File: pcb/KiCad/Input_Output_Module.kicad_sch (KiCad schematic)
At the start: 49 parts, among them J11 Curr_In (Out2), J12 Error_In, J13 Curr_Out (Out2), J14 Error_Out (In1), J16 Error_Mon, J3 Piezo_In (Out1), J5 Piezo_Out, J7 Piezo_Monitor, U4 OPA1604, U5 BUF634, U7 OPA1602, U8 OPA1602

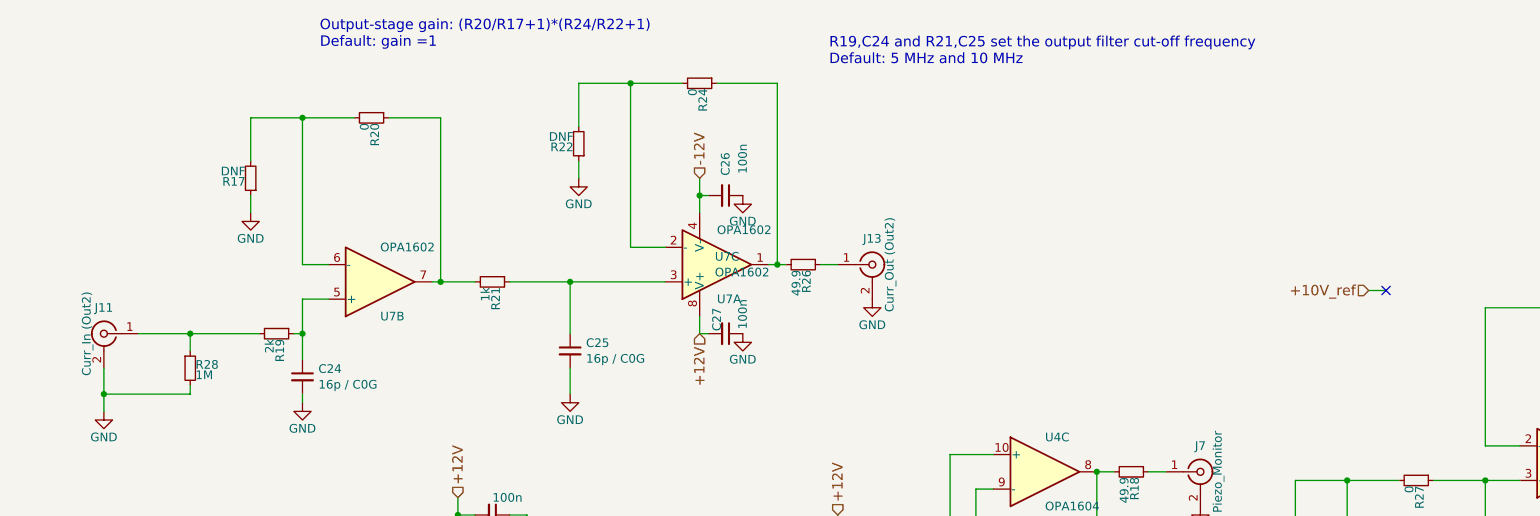
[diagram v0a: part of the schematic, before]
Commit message: Remove RedPitaya offset voltage at out2
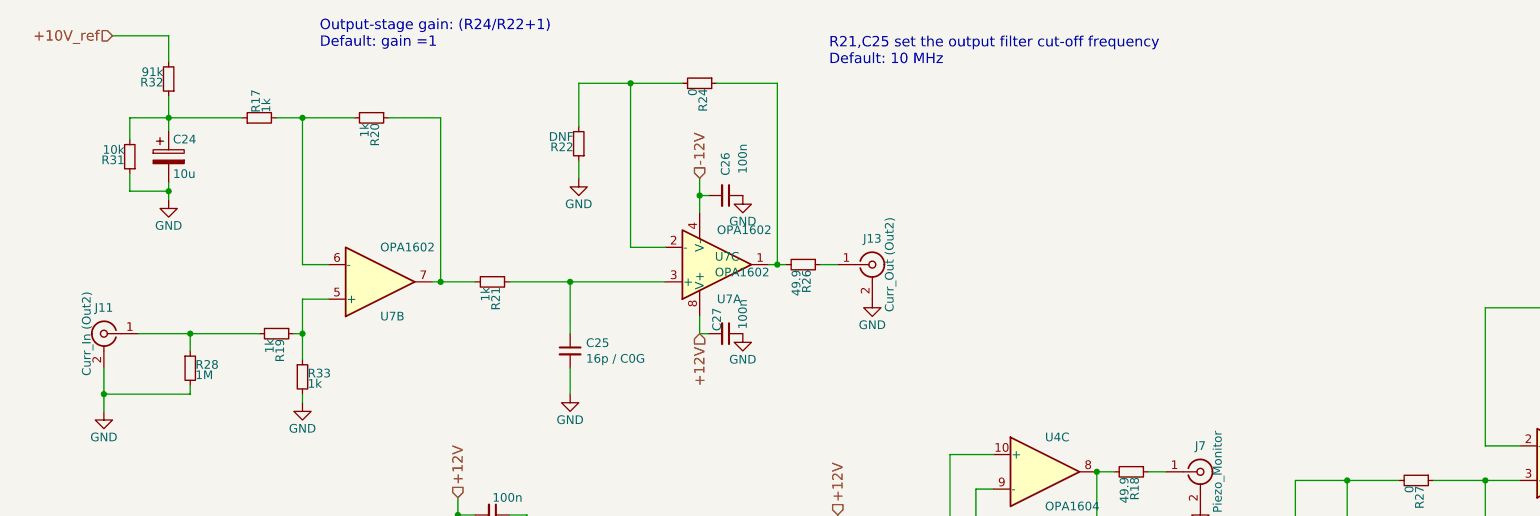
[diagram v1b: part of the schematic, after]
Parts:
- removed C24: 16p / C0G, Capacitor_SMD:C_0603_1608Metric, symbol Device:C_Small
- added C24: 10u, Capacitor_Tantalum_SMD:CP_EIA-3528-21_Kemet-B, symbol Device:C_Polarized
- added R31: 10k, Resistor_SMD:R_0603_1608Metric, symbol Device:R_Small
- added R32: 91k, Resistor_SMD:R_0603_1608Metric, symbol Device:R_Small
- added R33: 1k, Resistor_SMD:R_0603_1608Metric, symbol Device:R_Small
- R17: value DNF -> 1k; Config DNF -> (none); MFN (none) -> Susumu; PN (none) -> RR0816P-102-D
- R19: value 2k -> 1k; PN RR0816P-202-D -> RR0816P-102-D
- R20: value 0 -> 1k; MFN Vishay -> Susumu; PN CRCW06030000Z0EB -> RR0816P-102-D
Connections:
- net +10V_ref: now also R32.2
- net GND: now also C24.2, R31.1, R33.2; no longer R17.1
- net at R19.1, U7.5 (+): now also R33.1
- new net: C24.1, R17.1, R31.2, R32.1
- no-connect marks 1 -> 0
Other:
- note added: "Output-stage gain: (R24/R22+1) Default: gain =1"
- note added: "R21,C25 set the output filter cut-off frequency Default: 10 MHz"
- note removed: "Output-stage gain: (R20/R17+1)*(R24/R22+1) Default: gain =1"
- note removed: "R19,C24 and R21,C25 set the output filter cut-off frequency Default: 5 MHz and 10 MHz"

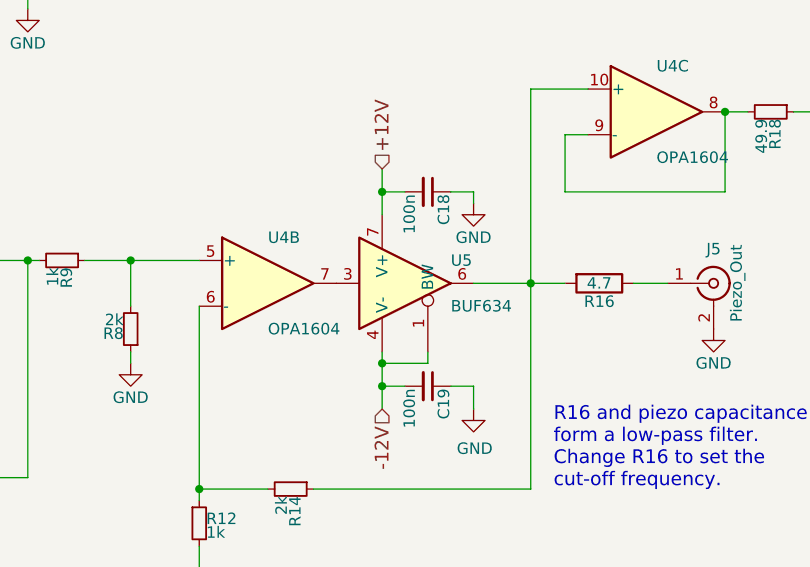
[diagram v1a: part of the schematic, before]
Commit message: Fix custom symbols. Update production files.
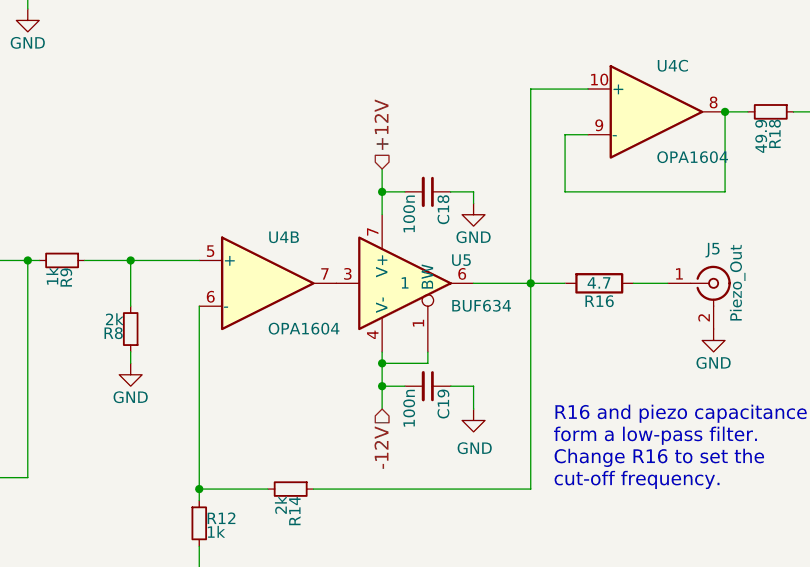
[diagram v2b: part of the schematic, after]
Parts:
- U5: Field4 (none) -> 1
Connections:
- now unconnected: U5.2, U5.5, U5.8
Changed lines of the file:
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@@
       (effects (font (size 1.27 1.27)) hide)
     )
+    (pin "1")
+    (pin "2")
+    (pin "3")
     (pin "5")
     (pin "6")
     (pin "7")
+    (pin "10")
+    (pin "8")
+    (pin "9")
+    (pin "12")
+    (pin "13")
+    (pin "14")
+    (pin "11")
+    (pin "4")
   )
   (symbol (lib_id "Device:C_Small") (at 83.82 90.17 270) (unit 1)
@@
       (effects (font (size 1.27 1.27)) hide)
     )
+    (property "Field4" "1" (id 6) (at 137.16 102.87 0))
     (pin "4")
     (pin "7")
@@
       (effects (font (size 1.27 1.27)) hide)
     )
+    (pin "1")
+    (pin "2")
+    (pin "3")
+    (pin "5")
+    (pin "6")
+    (pin "7")
     (pin "10")
     (pin "8")
     (pin "9")
+    (pin "12")
+    (pin "13")
+    (pin "14")
+    (pin "11")
+    (pin "4")
   )
   (symbol (lib_id "Device:R_Small") (at 177.8 83.82 270) (unit 1)
@@
     (pin "2")
     (pin "3")
+    (pin "5")
+    (pin "6")
+    (pin "7")
+    (pin "10")
+    (pin "8")
+    (pin "9")
+    (pin "12")
+    (pin "13")
+    (pin "14")
+    (pin "11")
+    (pin "4")
   )
   (symbol (lib_id "Device:C_Small") (at 83.82 110.49 270) (unit 1)
@@
       (effects (font (size 1.27 1.27)) hide)
     )
+    (pin "1")
+    (pin "2")
+    (pin "3")
+    (pin "5")
+    (pin "6")
+    (pin "7")
+    (pin "10")
+    (pin "8")
+    (pin "9")
     (pin "12")
     (pin "13")
     (pin "14")
+    (pin "11")
+    (pin "4")
   )
   (symbol (lib_id "Connector:Conn_Coaxial") (at 265.43 82.55 0) (unit 1)
@@
       (effects (font (size 1.27 1.27)) hide)
     )
+    (pin "1")
+    (pin "2")
+    (pin "3")
     (pin "5")
     (pin "6")
     (pin "7")
+    (pin "4")
+    (pin "8")
   )
   (symbol (lib_id "power:GND") (at 246.38 72.39 0) (unit 1)
@@
     (pin "2")
     (pin "3")
+    (pin "5")
+    (pin "6")
+    (pin "7")
+    (pin "4")
+    (pin "8")
   )
   (symbol (lib_id "Device:C_Small") (at 62.23 107.95 0) (mirror y) (unit 1)
@@
       (effects (font (size 1.27 1.27)) hide)
     )
+    (pin "1")
+    (pin "2")
+    (pin "3")
+    (pin "5")
+    (pin "6")
+    (pin "7")
+    (pin "10")
+    (pin "8")
+    (pin "9")
+    (pin "12")
+    (pin "13")
+    (pin "14")
     (pin "11")
     (pin "4")
@@
       (effects (font (size 1.27 1.27)) hide)
     )
+    (pin "1")
+    (pin "2")
+    (pin "3")
+    (pin "5")
+    (pin "6")
+    (pin "7")
     (pin "4")
     (pin "8")
@@
       (effects (font (size 1.27 1.27)) hide)
     )
+    (pin "1")
+    (pin "2")
+    (pin "3")
     (pin "5")
     (pin "6")
     (pin "7")
+    (pin "4")
+    (pin "8")
   )
   (symbol (lib_id "power:GND") (at 120.65 43.18 0) (unit 1)
@@
     (pin "2")
     (pin "3")
+    (pin "5")
+    (pin "6")
+    (pin "7")
+    (pin "4")
+    (pin "8")
   )
   (symbol (lib_id "Device:C_Small") (at 118.11 43.18 270) (unit 1)
@@
       (effects (font (size 1.27 1.27)) hide)
     )
+    (pin "1")
+    (pin "2")
+    (pin "3")
+    (pin "5")
+    (pin "6")
+    (pin "7")
     (pin "4")
     (pin "8")

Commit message: Update BOM
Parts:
- U5: Field4 1 -> (none)
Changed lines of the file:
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@@
       (effects (font (size 1.27 1.27)) hide)
     )
-    (property "Field4" "1" (id 6) (at 137.16 102.87 0))
     (pin "4")
     (pin "7")

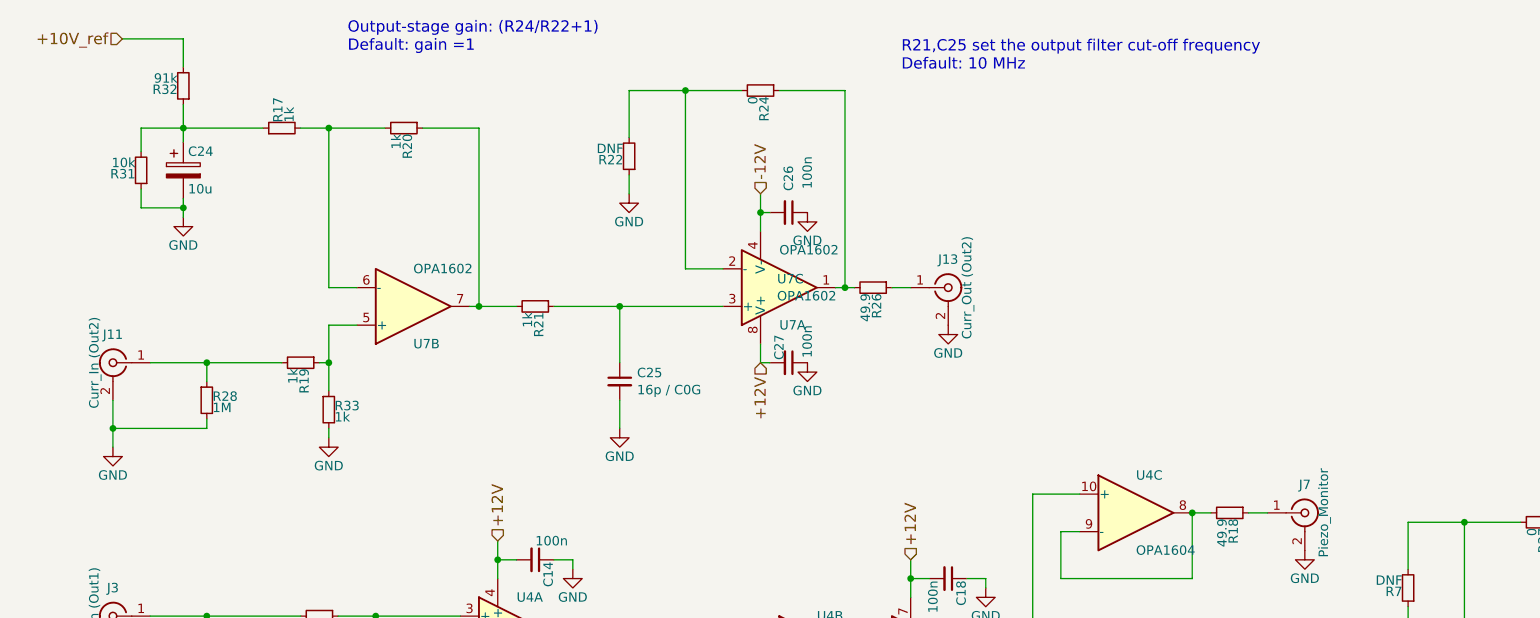
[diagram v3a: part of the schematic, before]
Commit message: Fix 'current' output stage.
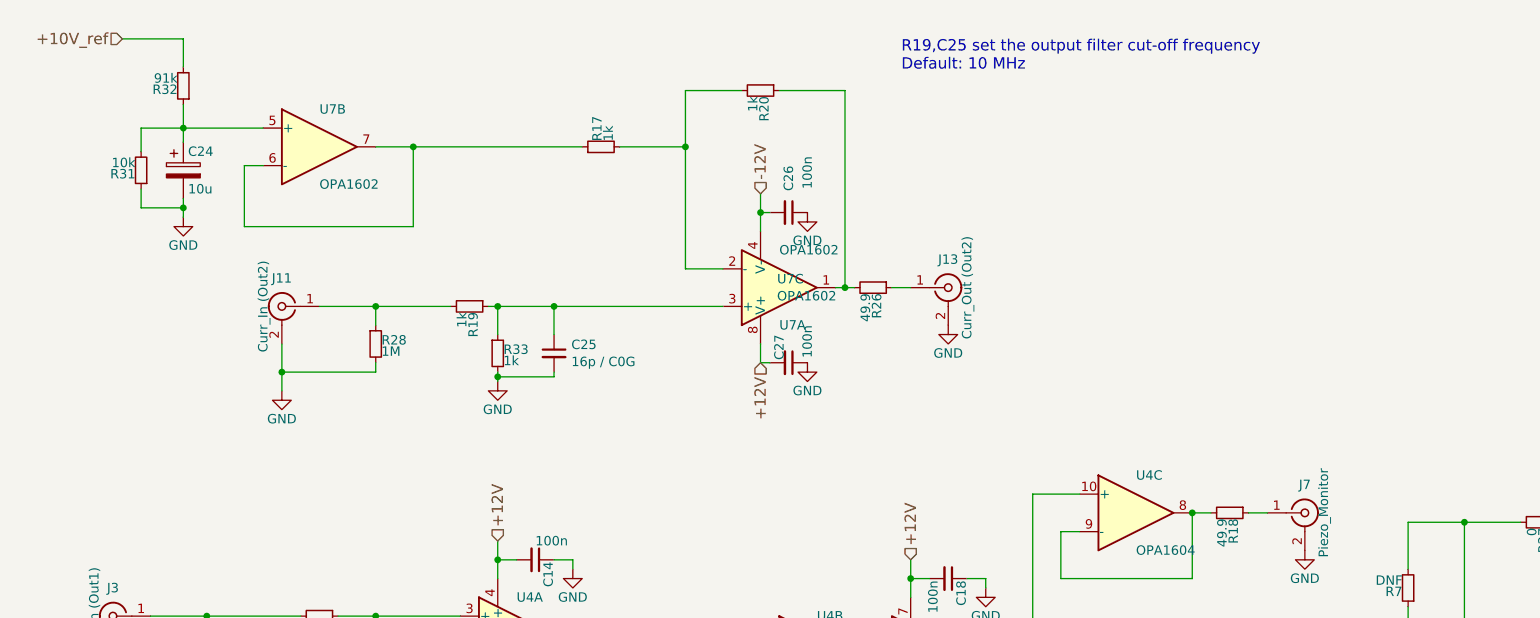
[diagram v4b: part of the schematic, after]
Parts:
- removed R21: 1k, Resistor_SMD:R_0603_1608Metric, symbol Device:R_Small
- removed R22: DNF, Resistor_SMD:R_0603_1608Metric, symbol Device:R_Small
- removed R24: 0, Resistor_SMD:R_0603_1608Metric, symbol Device:R_Small
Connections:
- net at R26.2, U7.1: now also R20.1
- net at R19.1, R33.1: now also C25.1, U7.3 (+); no longer U7.5 (+)
- net at R17.2, R20.2: now also U7.2 (-); no longer U7.6 (-)
- net at U7.7: now also R17.1, U7.6 (-); no longer R20.1
- net at C24.1, R31.2, R32.1: now also U7.5 (+); no longer R17.1
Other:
- note added: "R19,C25 set the output filter cut-off frequency Default: 10 MHz"
- note removed: "Output-stage gain: (R24/R22+1) Default: gain =1"
- note removed: "R21,C25 set the output filter cut-off frequency Default: 10 MHz"
- title: RedPitaya Lockbox: Piezo Controller -> RedPitaya Lockbox
- moved on the sheet: C25, J11, R17, R19, R20, R28, R33, U7B

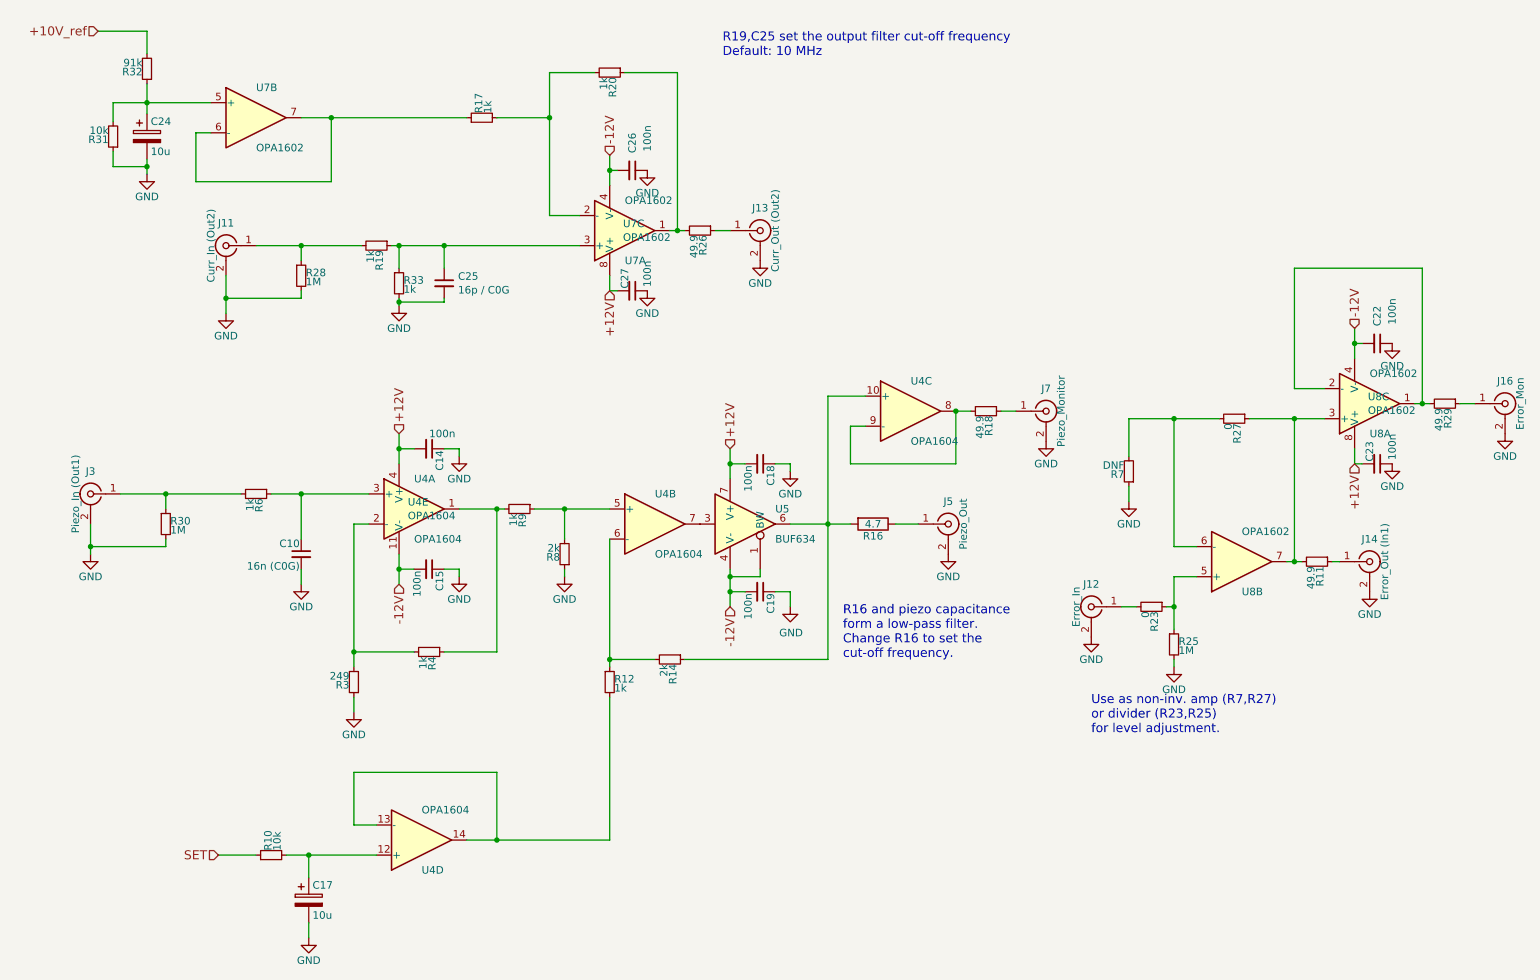
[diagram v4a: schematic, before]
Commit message: Updated to KiCAD 7 Cleaned up schematics Updated footprints Cleaned up PCB
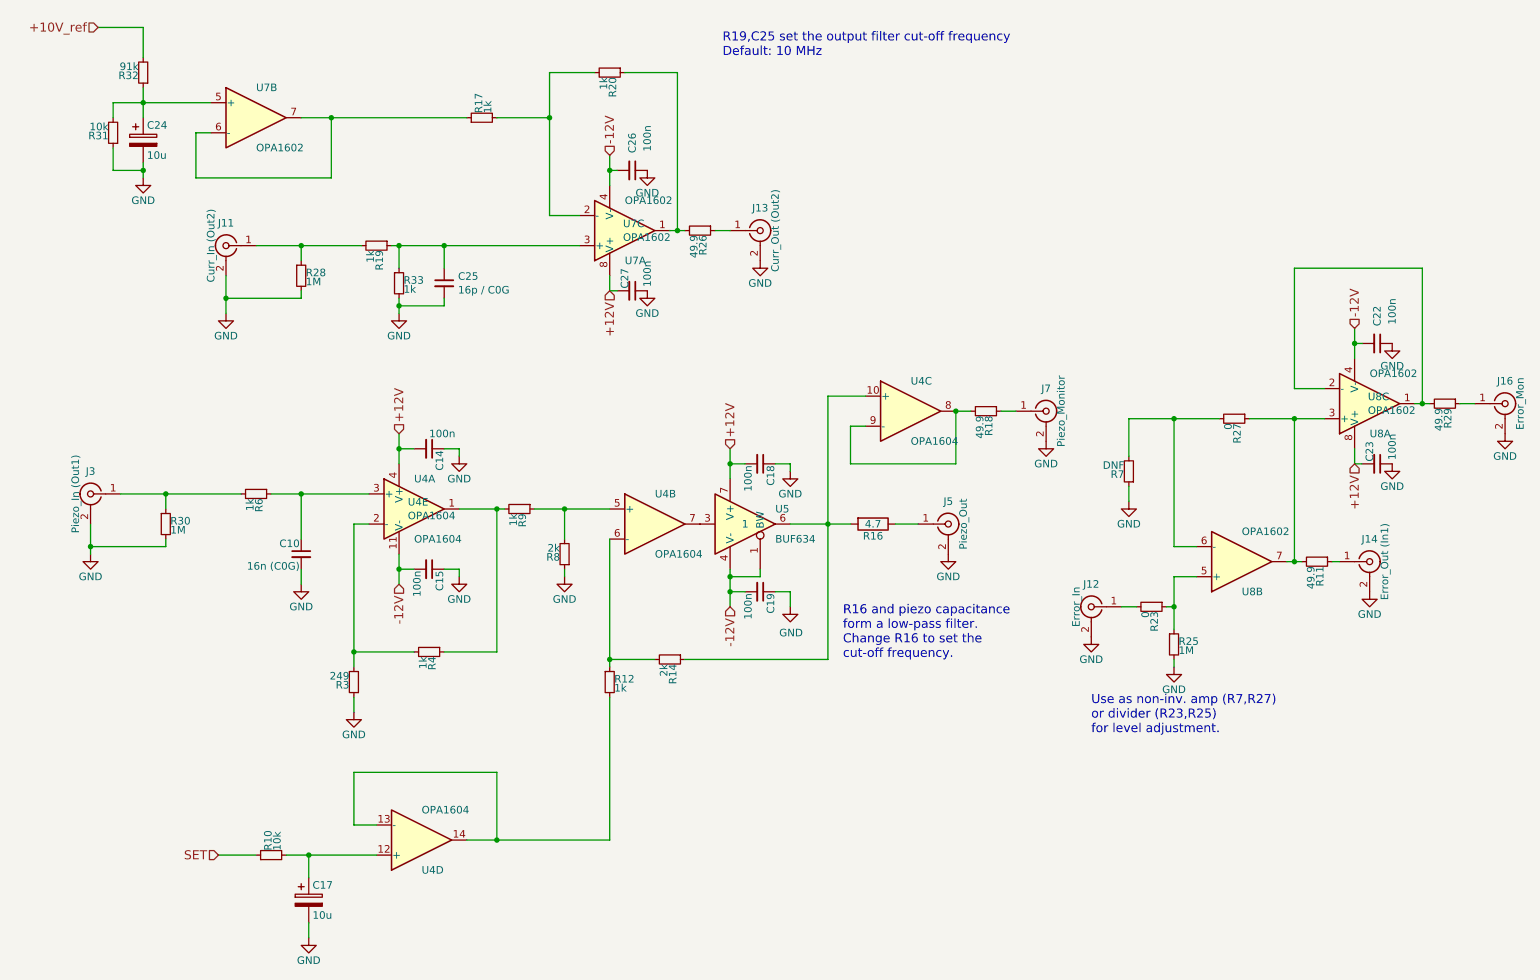
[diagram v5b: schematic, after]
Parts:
- U5: Field4 (none) -> 1; PN BUF634AIDR -> BUF634AIDR
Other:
- moved on the sheet: C24, R31, R32
